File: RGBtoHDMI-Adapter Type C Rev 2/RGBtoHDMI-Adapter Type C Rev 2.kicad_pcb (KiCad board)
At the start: 2 copper layers, 64.8 x 92.1 mm, 5 parts, among them J1 Conn_02x20_Odd_Even, J2 Conn_02x20_Odd_Even

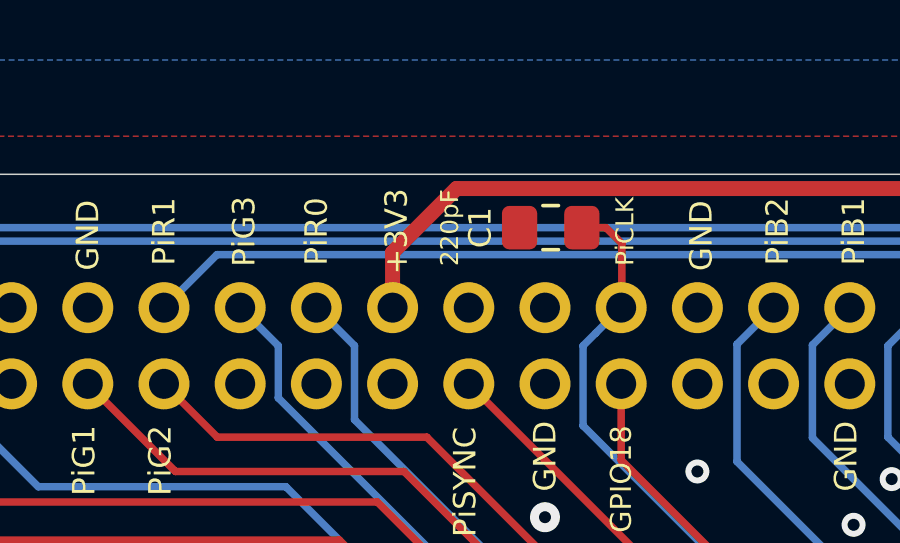
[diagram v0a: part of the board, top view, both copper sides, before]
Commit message: Updated cap value to 47pF
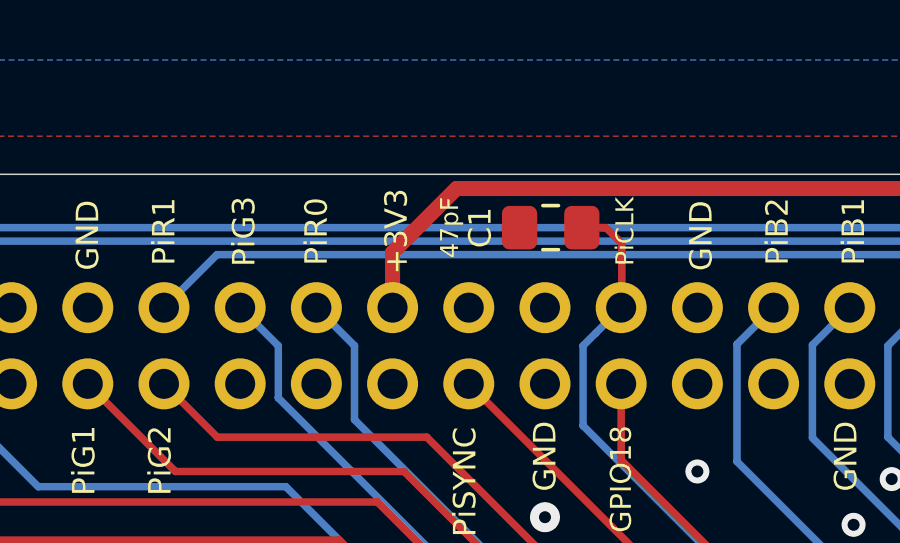
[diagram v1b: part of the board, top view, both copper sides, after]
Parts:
- C1: value 220pF -> 47pF
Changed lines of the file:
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@@
       (effects (font (size 0.75 0.75) (thickness 0.15)))
     )
-    (fp_text value 220pF (at -3.3655 0 90) (layer F.SilkS)
+    (fp_text value 47pF (at -3.3655 0 90) (layer F.SilkS)
       (effects (font (size 0.6 0.6) (thickness 0.15)))
     )
+    (fp_line (start -1 0.625) (end -1 -0.625) (layer F.Fab) (width 0.1))
+    (fp_line (start -1 -0.625) (end 1 -0.625) (layer F.Fab) (width 0.1))
+    (fp_line (start 1 -0.625) (end 1 0.625) (layer F.Fab) (width 0.1))
+    (fp_line (start 1 0.625) (end -1 0.625) (layer F.Fab) (width 0.1))
+    (fp_line (start -0.261252 -0.735) (end 0.261252 -0.735) (layer F.SilkS) (width 0.12))
+    (fp_line (start -0.261252 0.735) (end 0.261252 0.735) (layer F.SilkS) (width 0.12))
+    (fp_line (start -1.88 0.98) (end -1.88 -0.98) (layer F.CrtYd) (width 0.05))
+    (fp_line (start -1.88 -0.98) (end 1.88 -0.98) (layer F.CrtYd) (width 0.05))
+    (fp_line (start 1.88 -0.98) (end 1.88 0.98) (layer F.CrtYd) (width 0.05))
     (fp_line (start 1.88 0.98) (end -1.88 0.98) (layer F.CrtYd) (width 0.05))
-    (fp_line (start 1.88 -0.98) (end 1.88 0.98) (layer F.CrtYd) (width 0.05))
-    (fp_line (start -1.88 -0.98) (end 1.88 -0.98) (layer F.CrtYd) (width 0.05))
-    (fp_line (start -1.88 0.98) (end -1.88 -0.98) (layer F.CrtYd) (width 0.05))
-    (fp_line (start -0.261252 0.735) (end 0.261252 0.735) (layer F.SilkS) (width 0.12))
-    (fp_line (start -0.261252 -0.735) (end 0.261252 -0.735) (layer F.SilkS) (width 0.12))
-    (fp_line (start 1 0.625) (end -1 0.625) (layer F.Fab) (width 0.1))
-    (fp_line (start 1 -0.625) (end 1 0.625) (layer F.Fab) (width 0.1))
-    (fp_line (start -1 -0.625) (end 1 -0.625) (layer F.Fab) (width 0.1))
-    (fp_line (start -1 0.625) (end -1 -0.625) (layer F.Fab) (width 0.1))
     (fp_text user %R (at 0 0 -180) (layer F.Fab)
       (effects (font (size 0.5 0.5) (thickness 0.08)))
@@
       (effects (font (size 1 1) (thickness 0.15)) (justify mirror))
     )
+    (fp_line (start -3.81 1.254) (end 0.27 1.254) (layer B.Fab) (width 0.1))
+    (fp_line (start 1.27 0.254) (end 0.27 1.254) (layer B.Fab) (width 0.1))
+    (fp_line (start 1.27 0.254) (end 1.27 -49.53) (layer B.Fab) (width 0.1))
+    (fp_line (start 1.27 -49.53) (end -3.81 -49.53) (layer B.Fab) (width 0.1))
+    (fp_line (start -3.81 -49.53) (end -3.81 1.254) (layer B.Fab) (width 0.1))
+    (fp_line (start -3.87 1.27) (end -1.27 1.27) (layer B.SilkS) (width 0.12))
+    (fp_line (start -3.87 1.27) (end -3.87 -49.59) (layer B.SilkS) (width 0.12))
+    (fp_line (start -3.87 -49.59) (end 1.33 -49.59) (layer B.SilkS) (width 0.12))
+    (fp_line (start 1.33 -1.27) (end 1.33 -49.59) (layer B.SilkS) (width 0.12))
+    (fp_line (start -1.27 -1.27) (end 1.33 -1.27) (layer B.SilkS) (width 0.12))
+    (fp_line (start -1.27 1.27) (end -1.27 -1.27) (layer B.SilkS) (width 0.12))
+    (fp_line (start 1.33 1.27) (end 1.33 -0.06) (layer B.SilkS) (width 0.12))
+    (fp_line (start 0 1.27) (end 1.33 1.27) (layer B.SilkS) (width 0.12))
+    (fp_line (start -4.34 1.8) (end 1.76 1.8) (layer B.CrtYd) (width 0.05))
+    (fp_line (start 1.76 1.8) (end 1.76 -50) (layer B.CrtYd) (width 0.05))
+    (fp_line (start 1.76 -50) (end -4.34 -50) (layer B.CrtYd) (width 0.05))
     (fp_line (start -4.34 -50) (end -4.34 1.8) (layer B.CrtYd) (width 0.05))
-    (fp_line (start 1.76 -50) (end -4.34 -50) (layer B.CrtYd) (width 0.05))
-    (fp_line (start 1.76 1.8) (end 1.76 -50) (layer B.CrtYd) (width 0.05))
-    (fp_line (start -4.34 1.8) (end 1.76 1.8) (layer B.CrtYd) (width 0.05))
-    (fp_line (start 0 1.27) (end 1.33 1.27) (layer B.SilkS) (width 0.12))
-    (fp_line (start 1.33 1.27) (end 1.33 -0.06) (layer B.SilkS) (width 0.12))
-    (fp_line (start -1.27 1.27) (end -1.27 -1.27) (layer B.SilkS) (width 0.12))
-    (fp_line (start -1.27 -1.27) (end 1.33 -1.27) (layer B.SilkS) (width 0.12))
-    (fp_line (start 1.33 -1.27) (end 1.33 -49.59) (layer B.SilkS) (width 0.12))
-    (fp_line (start -3.87 -49.59) (end 1.33 -49.59) (layer B.SilkS) (width 0.12))
-    (fp_line (start -3.87 1.27) (end -3.87 -49.59) (layer B.SilkS) (width 0.12))
-    (fp_line (start -3.87 1.27) (end -1.27 1.27) (layer B.SilkS) (width 0.12))
-    (fp_line (start -3.81 -49.53) (end -3.81 1.254) (layer B.Fab) (width 0.1))
-    (fp_line (start 1.27 -49.53) (end -3.81 -49.53) (layer B.Fab) (width 0.1))
-    (fp_line (start 1.27 0.254) (end 1.27 -49.53) (layer B.Fab) (width 0.1))
-    (fp_line (start 1.27 0.254) (end 0.27 1.254) (layer B.Fab) (width 0.1))
-    (fp_line (start -3.81 1.254) (end 0.27 1.254) (layer B.Fab) (width 0.1))
     (fp_text user %R (at -1.27 -24.13 180) (layer B.Fab) hide
       (effects (font (size 1 1) (thickness 0.15)) (justify mirror))
@@
       (effects (font (size 1 1) (thickness 0.15)))
     )
+    (fp_circle (center 0 0) (end 3.1 0) (layer F.CrtYd) (width 0.05))
     (fp_circle (center 0 0) (end 2.85 0) (layer Cmts.User) (width 0.15))
-    (fp_circle (center 0 0) (end 3.1 0) (layer F.CrtYd) (width 0.05))
     (fp_text user %R (at 0.3 0) (layer F.Fab) hide
       (effects (font (size 1 1) (thickness 0.15)))
@@
       (effects (font (size 1 1) (thickness 0.15)))
     )
+    (fp_circle (center 0 0) (end 3.1 0) (layer F.CrtYd) (width 0.05))
     (fp_circle (center 0 0) (end 2.85 0) (layer Cmts.User) (width 0.15))
-    (fp_circle (center 0 0) (end 3.1 0) (layer F.CrtYd) (width 0.05))
     (fp_text user %R (at 0.3 0) (layer F.Fab) hide
       (effects (font (size 1 1) (thickness 0.15)))
@@
       (effects (font (size 1 1) (thickness 0.15)) (justify mirror))
     )
+    (fp_line (start 0 1.27) (end 3.81 1.27) (layer B.Fab) (width 0.1))
+    (fp_line (start 3.81 1.27) (end 3.81 -49.53) (layer B.Fab) (width 0.1))
+    (fp_line (start 3.81 -49.53) (end -1.27 -49.53) (layer B.Fab) (width 0.1))
+    (fp_line (start -1.27 -49.53) (end -1.27 0) (layer B.Fab) (width 0.1))
+    (fp_line (start -1.27 0) (end 0 1.27) (layer B.Fab) (width 0.1))
+    (fp_line (start -1.33 -49.59) (end 3.87 -49.59) (layer B.SilkS) (width 0.12))
+    (fp_line (start -1.33 -1.27) (end -1.33 -49.59) (layer B.SilkS) (width 0.12))
+    (fp_line (start 3.87 1.33) (end 3.87 -49.59) (layer B.SilkS) (width 0.12))
+    (fp_line (start -1.33 -1.27) (end 1.27 -1.27) (layer B.SilkS) (width 0.12))
+    (fp_line (start 1.27 -1.27) (end 1.27 1.33) (layer B.SilkS) (width 0.12))
+    (fp_line (start 1.27 1.33) (end 3.87 1.33) (layer B.SilkS) (width 0.12))
+    (fp_line (start -1.33 0) (end -1.33 1.33) (layer B.SilkS) (width 0.12))
+    (fp_line (start -1.33 1.33) (end 0 1.33) (layer B.SilkS) (width 0.12))
+    (fp_line (start -1.8 1.8) (end -1.8 -50.05) (layer B.CrtYd) (width 0.05))
+    (fp_line (start -1.8 -50.05) (end 4.35 -50.05) (layer B.CrtYd) (width 0.05))
+    (fp_line (start 4.35 -50.05) (end 4.35 1.8) (layer B.CrtYd) (width 0.05))
     (fp_line (start 4.35 1.8) (end -1.8 1.8) (layer B.CrtYd) (width 0.05))
-    (fp_line (start 4.35 -50.05) (end 4.35 1.8) (layer B.CrtYd) (width 0.05))
-    (fp_line (start -1.8 -50.05) (end 4.35 -50.05) (layer B.CrtYd) (width 0.05))
-    (fp_line (start -1.8 1.8) (end -1.8 -50.05) (layer B.CrtYd) (width 0.05))
-    (fp_line (start -1.33 1.33) (end 0 1.33) (layer B.SilkS) (width 0.12))
-    (fp_line (start -1.33 0) (end -1.33 1.33) (layer B.SilkS) (width 0.12))
-    (fp_line (start 1.27 1.33) (end 3.87 1.33) (layer B.SilkS) (width 0.12))
-    (fp_line (start 1.27 -1.27) (end 1.27 1.33) (layer B.SilkS) (width 0.12))
-    (fp_line (start -1.33 -1.27) (end 1.27 -1.27) (layer B.SilkS) (width 0.12))
-    (fp_line (start 3.87 1.33) (end 3.87 -49.59) (layer B.SilkS) (width 0.12))
-    (fp_line (start -1.33 -1.27) (end -1.33 -49.59) (layer B.SilkS) (width 0.12))
-    (fp_line (start -1.33 -49.59) (end 3.87 -49.59) (layer B.SilkS) (width 0.12))
-    (fp_line (start -1.27 0) (end 0 1.27) (layer B.Fab) (width 0.1))
-    (fp_line (start -1.27 -49.53) (end -1.27 0) (layer B.Fab) (width 0.1))
-    (fp_line (start 3.81 -49.53) (end -1.27 -49.53) (layer B.Fab) (width 0.1))
-    (fp_line (start 3.81 1.27) (end 3.81 -49.53) (layer B.Fab) (width 0.1))
-    (fp_line (start 0 1.27) (end 3.81 1.27) (layer B.Fab) (width 0.1))
     (fp_text user %R (at 1.27 -24.13 270) (layer B.Fab)
       (effects (font (size 1 1) (thickness 0.15)) (justify mirror))
